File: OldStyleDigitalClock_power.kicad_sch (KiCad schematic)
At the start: 24 parts, among them J1 USB_A_OUT, J2 USB_A_OUT, J3 USB_C_IN, U11 NE555D

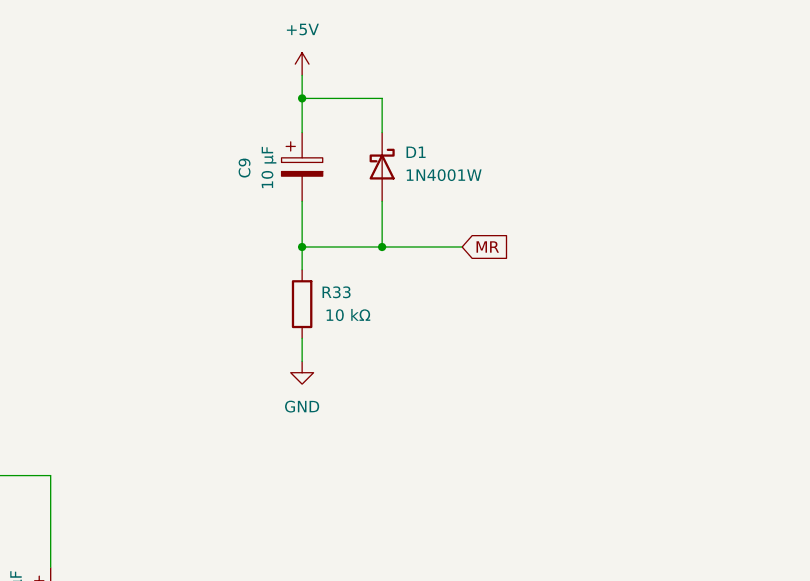
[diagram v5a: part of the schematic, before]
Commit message: Fixed issue in MR circuit. More tracks.
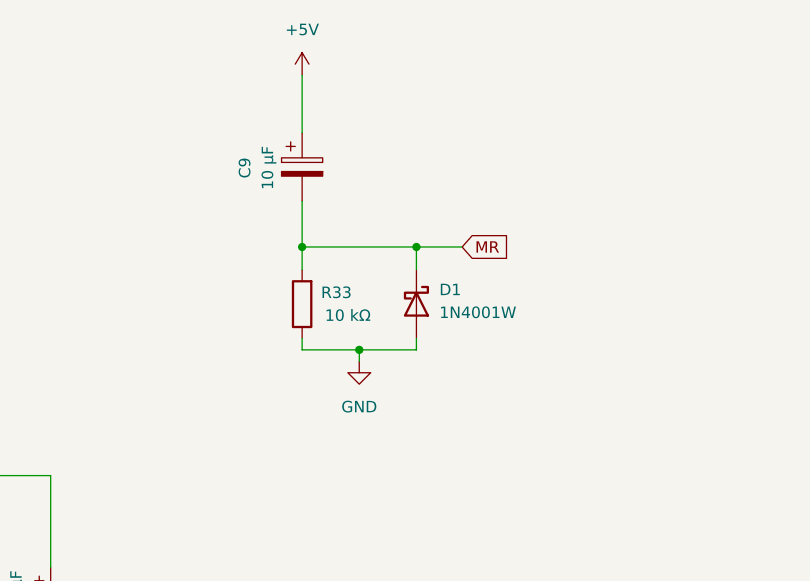
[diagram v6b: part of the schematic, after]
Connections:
- net +5V: no longer D1.1 (K)
- net GND: now also D1.2 (A)
- net MR: now also D1.1 (K); no longer D1.2 (A)
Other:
- moved on the sheet: D1
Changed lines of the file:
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@@
-	)
-	(junction
-		(at 116.84 27.94)
-		(diameter 0)
-		(color 0 0 0 0)
 	)
 	(junction
@@
 	)
 	(junction
-		(at 125.73 44.45)
+		(at 78.74 109.22)
 		(diameter 0)
 		(color 0 0 0 0)
 	)
 	(junction
-		(at 78.74 109.22)
+		(at 129.54 44.45)
 		(diameter 0)
 		(color 0 0 0 0)
@@
 	)
 	(junction
+		(at 123.19 55.88)
+		(diameter 0)
+		(color 0 0 0 0)
+	)
+	(junction
 		(at 33.02 50.8)
 		(diameter 0)
@@
 	(wire
 		(pts
-			(xy 125.73 39.37) (xy 125.73 44.45)
-		)
-		(stroke
-			(width 0)
-			(type default)
-		)
-	)
-	(wire
-		(pts
 			(xy 165.1 92.71) (xy 180.34 92.71)
 		)
@@
 	(wire
 		(pts
-			(xy 125.73 44.45) (xy 116.84 44.45)
+			(xy 116.84 44.45) (xy 129.54 44.45)
 		)
 		(stroke
@@
 	(wire
 		(pts
+			(xy 129.54 55.88) (xy 123.19 55.88)
+		)
+		(stroke
+			(width 0)
+			(type default)
+		)
+	)
+	(wire
+		(pts
 			(xy 132.08 92.71) (xy 128.27 92.71)
 		)
@@
 	(wire
 		(pts
-			(xy 134.62 44.45) (xy 125.73 44.45)
+			(xy 123.19 55.88) (xy 123.19 57.15)
 		)
 		(stroke
@@
 	(wire
 		(pts
-			(xy 116.84 54.61) (xy 116.84 57.15)
-		)
-		(stroke
-			(width 0)
-			(type default)
-		)
-	)
-	(wire
-		(pts
-			(xy 116.84 25.4) (xy 116.84 27.94)
+			(xy 116.84 54.61) (xy 116.84 55.88)
+		)
+		(stroke
+			(width 0)
+			(type default)
+		)
+	)
+	(wire
+		(pts
+			(xy 116.84 25.4) (xy 116.84 31.75)
 		)
 		(stroke
@@
 	(wire
 		(pts
-			(xy 116.84 27.94) (xy 116.84 31.75)
-		)
-		(stroke
-			(width 0)
-			(type default)
-		)
-	)
-	(wire
-		(pts
 			(xy 217.17 105.41) (xy 223.52 105.41)
 		)
@@
 	(wire
 		(pts
-			(xy 125.73 27.94) (xy 116.84 27.94)
-		)
-		(stroke
-			(width 0)
-			(type default)
-		)
-	)
-	(wire
-		(pts
 			(xy 60.96 35.56) (xy 62.23 35.56)
 		)
@@
 	(wire
 		(pts
+			(xy 129.54 54.61) (xy 129.54 55.88)
+		)
+		(stroke
+			(width 0)
+			(type default)
+		)
+	)
+	(wire
+		(pts
+			(xy 129.54 44.45) (xy 134.62 44.45)
+		)
+		(stroke
+			(width 0)
+			(type default)
+		)
+	)
+	(wire
+		(pts
 			(xy 189.23 63.5) (xy 194.31 63.5)
 		)
@@
 	(wire
 		(pts
-			(xy 125.73 27.94) (xy 125.73 31.75)
-		)
-		(stroke
-			(width 0)
-			(type default)
-		)
-	)
-	(wire
-		(pts
 			(xy 165.1 92.71) (xy 165.1 99.06)
 		)
@@
 	(wire
 		(pts
+			(xy 123.19 55.88) (xy 116.84 55.88)
+		)
+		(stroke
+			(width 0)
+			(type default)
+		)
+	)
+	(wire
+		(pts
 			(xy 53.34 50.8) (xy 53.34 53.34)
 		)
@@
 		(pts
 			(xy 64.77 87.63) (xy 64.77 109.22)
+		)
+		(stroke
+			(width 0)
+			(type default)
+		)
+	)
+	(wire
+		(pts
+			(xy 129.54 44.45) (xy 129.54 46.99)
 		)
 		(stroke
@@
 	(symbol
 		(lib_id "Diode:BAT85")
-		(at 125.73 35.56 270)
+		(at 129.54 50.8 270)
 		(unit 1)
 		(exclude_from_sim no)
@@
 		(fields_autoplaced yes)
 		(property "Reference" "D1"
-			(at 128.27 33.9724 90)
+			(at 132.08 49.2124 90)
 			(effects
 				(font
@@
 		)
 		(property "Value" "1N4001W"
-			(at 128.27 36.5124 90)
+			(at 132.08 51.7524 90)
 			(effects
 				(font
@@
 		)
 		(property "Footprint" "Diode_SMD:D_SOD-123"
-			(at 121.285 35.56 0)
+			(at 125.095 50.8 0)
 			(effects
 				(font
@@
 		)
 		(property "Datasheet" "https://assets.nexperia.com/documents/data-sheet/BAT85.pdf"
-			(at 125.73 35.56 0)
+			(at 129.54 50.8 0)
 			(effects
 				(font
@@
 		)
 		(property "Description" ""
-			(at 125.73 35.56 0)
+			(at 129.54 50.8 0)
 			(effects
 				(font
@@
 	(symbol
 		(lib_id "power:GND")
-		(at 116.84 57.15 0)
+		(at 123.19 57.15 0)
 		(unit 1)
 		(exclude_from_sim no)
@@
 		(dnp no)
 		(property "Reference" "#PWR035"
-			(at 116.84 63.5 0)
+			(at 123.19 63.5 0)
 			(effects
 				(font
@@
 		)
 		(property "Value" "GND"
-			(at 116.84 62.23 0)
+			(at 123.19 62.23 0)
 			(effects
 				(font
@@
 		)
 		(property "Footprint" ""
-			(at 116.84 57.15 0)
+			(at 123.19 57.15 0)
 			(effects
 				(font
@@
 		)
 		(property "Datasheet" ""
-			(at 116.84 57.15 0)
+			(at 123.19 57.15 0)
 			(effects
 				(font
@@
 		)
 		(property "Description" ""
-			(at 116.84 57.15 0)
-			(effects
-				(font
+			(at 123.19 57.15 0)
+			(effects
+				(font

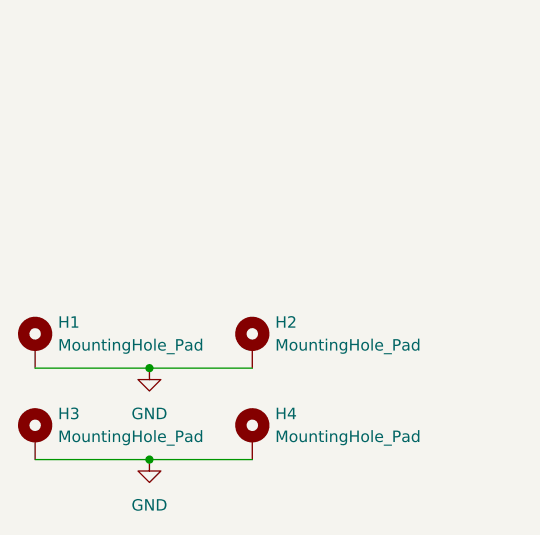
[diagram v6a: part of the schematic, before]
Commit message: Tracks, first draft completed prior to design review
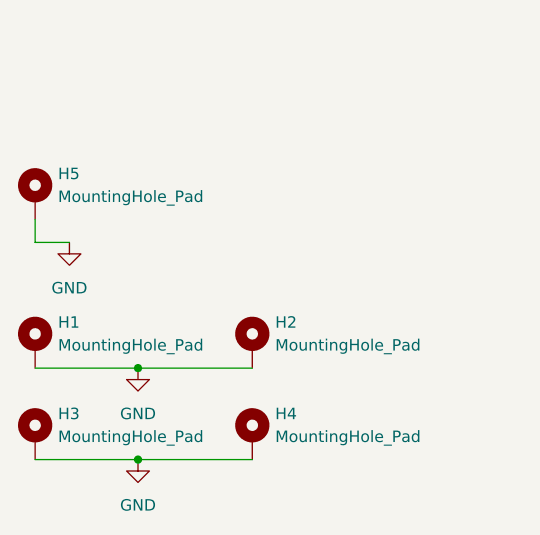
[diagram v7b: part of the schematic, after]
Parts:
- added H5: MountingHole_Pad, symbol Mechanical:MountingHole_Pad
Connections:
- net GND: now also H5.1

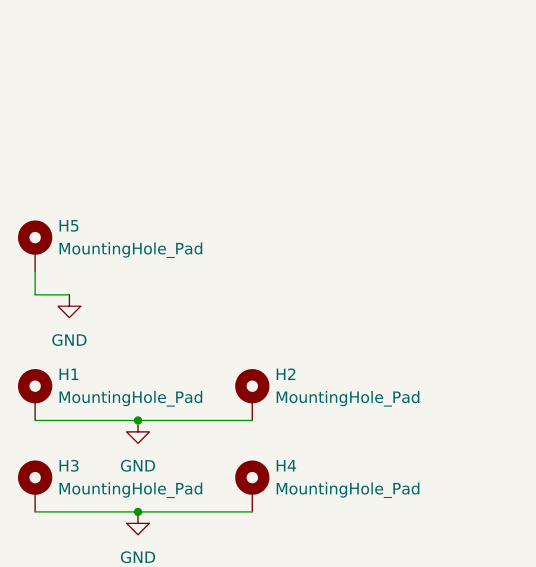
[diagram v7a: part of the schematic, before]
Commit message: connected mounting holes to GND
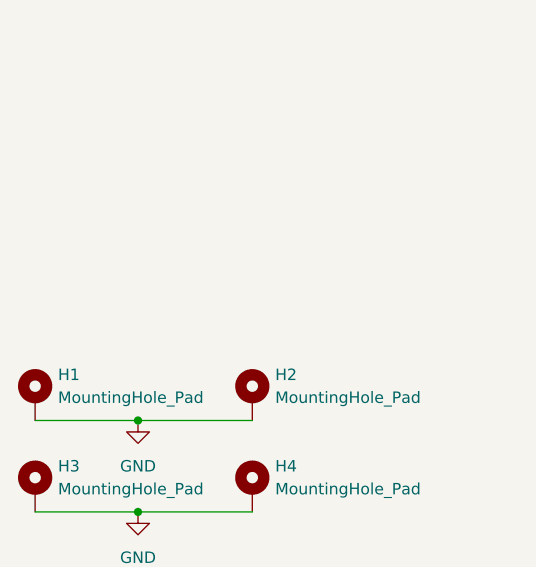
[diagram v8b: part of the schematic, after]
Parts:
- removed H5: MountingHole_Pad, symbol Mechanical:MountingHole_Pad
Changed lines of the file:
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@@
-	(wire
-		(pts
-			(xy 29.21 161.29) (xy 25.4 161.29)
-		)
-		(stroke
-			(width 0)
-			(type default)
-		)
-	)
 	(wire
 		(pts
@@
 		(pts
 			(xy 62.23 43.18) (xy 60.96 43.18)
-		)
-		(stroke
-			(width 0)
-			(type default)
-		)
-	)
-	(wire
-		(pts
-			(xy 25.4 161.29) (xy 25.4 158.75)
 		)
 		(stroke
@@
 	)
 	(symbol
-		(lib_id "Mechanical:MountingHole_Pad")
-		(at 25.4 156.21 0)
-		(unit 1)
-		(exclude_from_sim no)
-		(in_bom no)
-		(on_board yes)
-		(dnp no)
-		(fields_autoplaced yes)
-		(property "Reference" "H5"
-			(at 27.94 153.6699 0)
-			(effects
-				(font
-					(size 1.27 1.27)
-				)
-				(justify left)
-			)
-		)
-		(property "Value" "MountingHole_Pad"
-			(at 27.94 156.2099 0)
-			(effects
-				(font
-					(size 1.27 1.27)
-				)
-				(justify left)
-			)
-		)
-		(property "Footprint" ""
-			(at 25.4 156.21 0)
-			(effects
-				(font
-					(size 1.27 1.27)
-				)
-				(hide yes)
-			)
-		)
-		(property "Datasheet" "~"
-			(at 25.4 156.21 0)
-			(effects
-				(font
-					(size 1.27 1.27)
-				)
-				(hide yes)
-			)
-		)
-		(property "Description" "Mounting Hole with connection"
-			(at 25.4 156.21 0)
-			(effects
-				(font
-					(size 1.27 1.27)
-				)
-				(hide yes)
-			)
-		)
-		(pin "1"
-		)
-		(instances
-			(project ""
-				(path "/a24f1d5b-eb61-47a3-9a92-6515e74f7a21/31b03831-3d01-49ef-8f86-173fa6c5d953"
-					(reference "H5")
-					(unit 1)
-				)
-			)
-		)
-	)
-	(symbol
 		(lib_id "Connector:USB_C_Receptacle_USB2.0_16P")
 		(at 39.37 85.09 0)
@@
 					(unit 1)
 				)
-			)
-		)
-	)
-	(symbol
-		(lib_id "power:GND")
-		(at 29.21 161.29 0)
-		(unit 1)
-		(exclude_from_sim no)
-		(in_bom yes)
-		(on_board yes)
-		(dnp no)
-		(fields_autoplaced yes)
-		(property "Reference" "#PWR062"
-			(at 29.21 167.64 0)
-			(effects
-				(font
-					(size 1.27 1.27)
-				)
-				(hide yes)
-			)
-		)
-		(property "Value" "GND"
-			(at 29.21 166.37 0)
-			(effects
-				(font
-					(size 1.27 1.27)
-				)
-			)
-		)
-		(property "Footprint" ""
-			(at 29.21 161.29 0)
-			(effects
-				(font
-					(size 1.27 1.27)
-				)
-				(hide yes)
-			)
-		)
-		(property "Datasheet" ""
-			(at 29.21 161.29 0)
-			(effects
-				(font
-					(size 1.27 1.27)
-				)
-				(hide yes)
-			)
-		)
-		(property "Description" ""
-			(at 29.21 161.29 0)
-			(effects
-				(font
-					(size 1.27 1.27)
-				)
-			)
-		)
-		(pin "1"
-		)
-		(instances
-			(project "OldStyleDigitalClock"
-				(path "/a24f1d5b-eb61-47a3-9a92-6515e74f7a21/31b03831-3d01-49ef-8f86-173fa6c5d953"
-					(reference "#PWR062")
-					(unit 1)
-				)
